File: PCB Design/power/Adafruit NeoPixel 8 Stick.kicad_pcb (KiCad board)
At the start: 2 copper layers, 34.6 x 37.8 mm, 2 parts, among them CN2 1X4SMT

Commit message: finished power supply
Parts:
- added J1: PJ-102AH, PJ-102AH:PJ-102AH, F.Cu at (131.3, 111.8)
- moved C1 20.8 mm to (146.3, 117.9)
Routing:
- net +5V: track 0.00 -> 47.6 mm, vias 0 -> 1
- added copper zone on B.Cu, net GND
- added copper zone on F.Cu, net GND

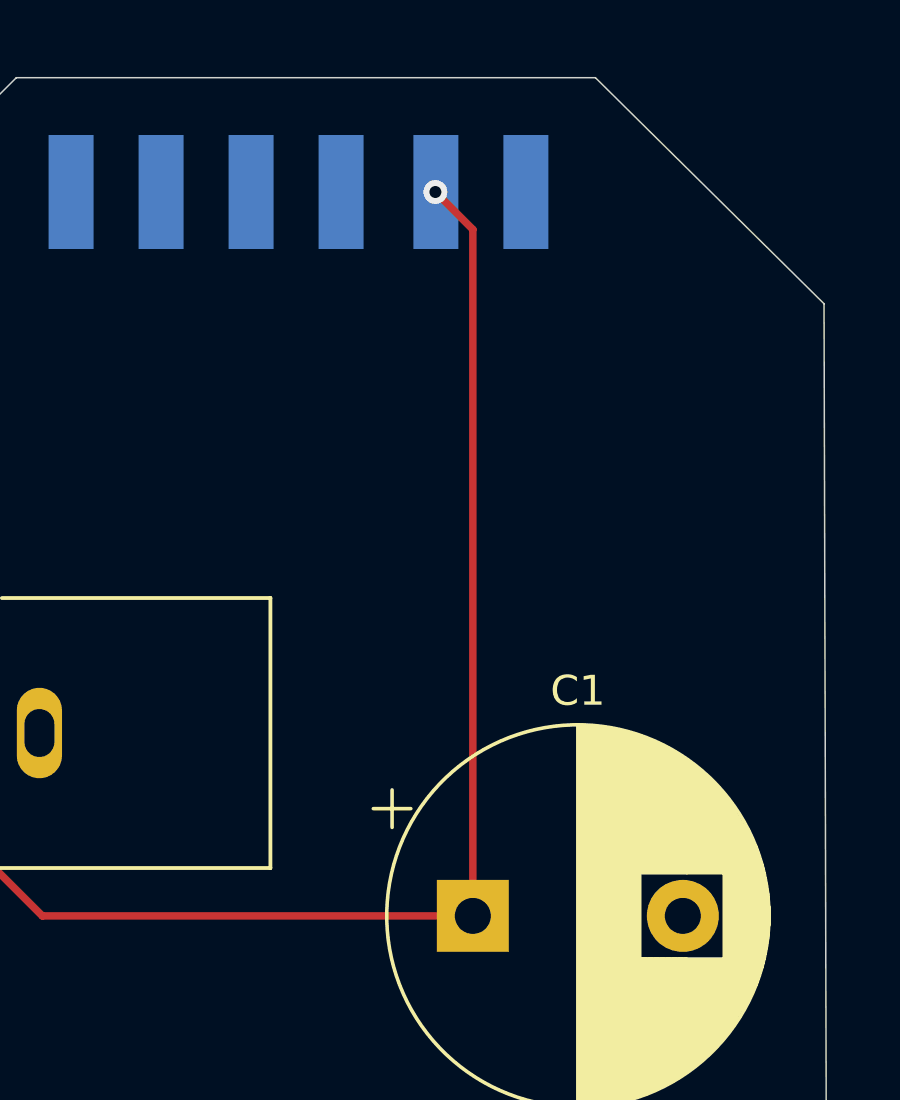
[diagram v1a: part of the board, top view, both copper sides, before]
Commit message: move vias off pads
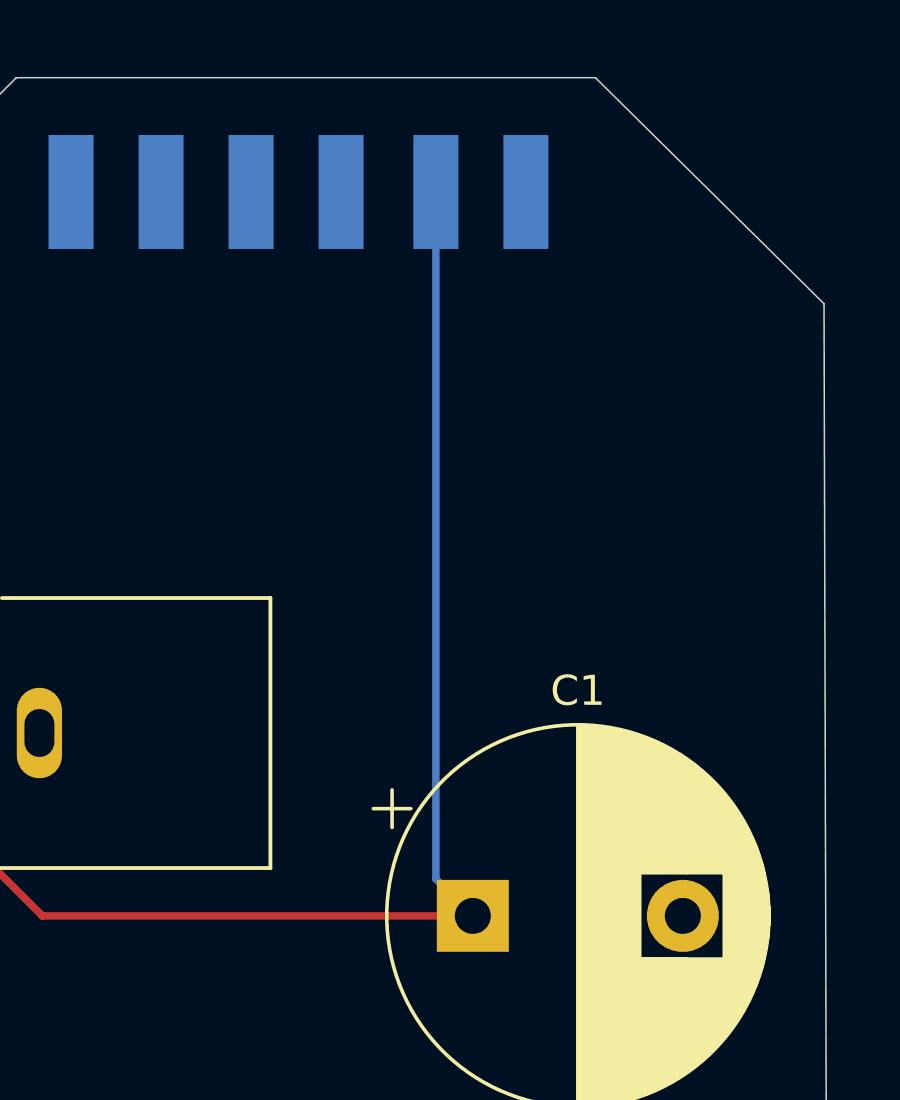
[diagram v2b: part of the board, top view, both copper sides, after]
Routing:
- net +5V: vias 1 -> 0
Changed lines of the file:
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@@
   (gr_line (start 122.428 97.536) (end 130.048 89.915998) (layer "Edge.Cuts") (width 0.05))
   (segment (start 130.914 117.856) (end 145.266041 117.856) (width 0.25) (layer "F.Cu") (net 1))
-  (segment (start 145.266041 94.974041) (end 144.018 93.726) (width 0.25) (layer "F.Cu") (net 1))
   (segment (start 124.818 111.76) (end 130.914 117.856) (width 0.25) (layer "F.Cu") (net 1))
-  (segment (start 145.266041 117.856) (end 145.266041 94.974041) (width 0.25) (layer "F.Cu") (net 1))
-  (via (at 144.018 93.726) (size 0.8) (drill 0.4) (layers "F.Cu" "B.Cu") (net 1))
+  (segment (start 144.034 116.623959) (end 145.266041 117.856) (width 0.25) (layer "B.Cu") (net 1))
+  (segment (start 144.034 93.726) (end 144.034 116.623959) (width 0.25) (layer "B.Cu") (net 1))
   (zone (net 2) (net_name "GND") (layers F&B.Cu) (hatch edge 0.508)
     (connect_pads (clearance 0.000001))
